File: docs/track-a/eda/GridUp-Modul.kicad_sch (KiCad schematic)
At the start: 54 parts, among them J1 İç ihtiyaç L / N / PE, J2 CT L1, J3 CT L2, J4 CT L3, J5 CT nötr, J6 Genişleme 2×5, J7 RS-485 klemens B / GND / A, J8 SMA panel, J9 Servis USB/UART0, SW1 Reset, U1 ESP32-S3-WROOM-1U-N8, U2 MLX90640ESF-BAA, U3 SHT31-DIS-B, U4 MAX3485, U5 RAC05-05SK/277, U6 AP7361C-33E 3,3 V / 1 A, U7 TPS61099 4,6 V

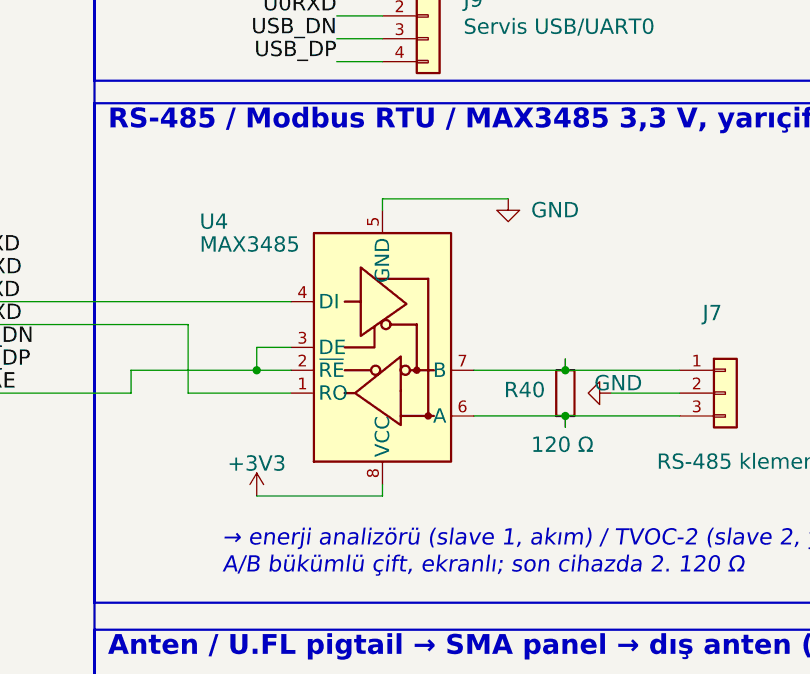
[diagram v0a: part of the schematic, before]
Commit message: İZ A: 03 — MAX3485 için sade kutu sembol (GridUp:MAX3485, aynı pin numaraları; kütüphane sembolü aynalanınca içi karışıyordu), ayna kaldırıldı, VCC üst / GND alt; ERC 0/0, netlist 103/103
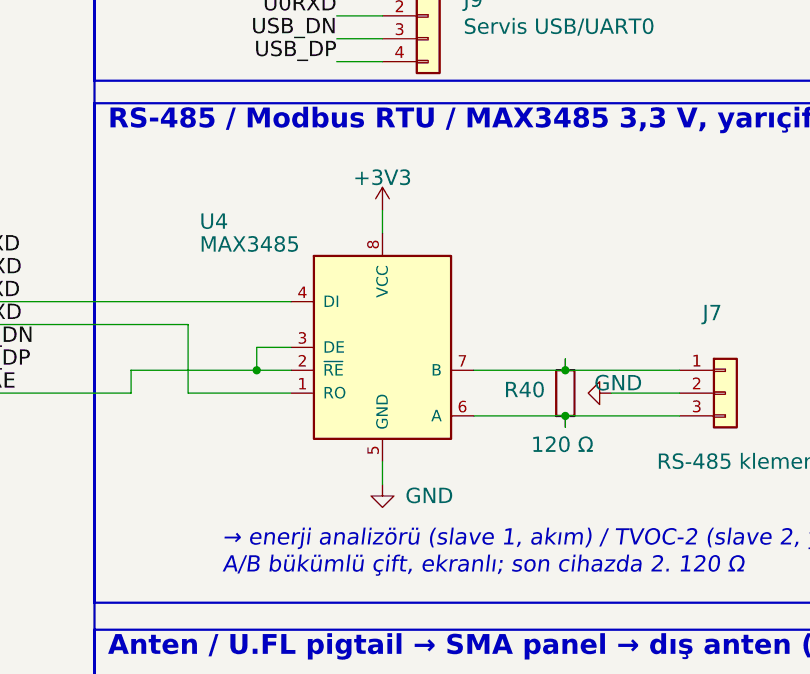
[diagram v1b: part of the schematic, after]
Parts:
- removed U4: MAX3485, Package_SO:SOIC-8_3.9x4.9mm_P1.27mm, symbol Interface_UART:MAX3485
- added U4: MAX3485, Package_SO:SOIC-8_3.9x4.9mm_P1.27mm, symbol GridUp:MAX3485
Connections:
- net +3V3: now also U4.8 (VCC)
- net DE_RE: now also U4.2 (~{RE}), U4.3 (DE)
- net GND: now also U4.5 (GND)
- net U1RXD: now also U4.1 (RO)
- net U1TXD: now also U4.4 (DI)
- net at J7.1 (Pin_1), R40.1: now also U4.7 (B)
- net at J7.3 (Pin_3), R40.2: now also U4.6 (A)
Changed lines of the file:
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@@
 	(wire
 		(pts
+			(xy 254 74.93)
 			(xy 254 72.39)
-			(xy 254 71.12)
-		)
-		(stroke
-			(width 0)
-			(type default)
-			(color 70 70 70 1)
-		)
-	)
-	(wire
-		(pts
-			(xy 254 71.12)
-			(xy 267.97 71.12)
-		)
-		(stroke
-			(width 0)
-			(type default)
-			(color 70 70 70 1)
-		)
-	)
-	(wire
-		(pts
-			(xy 254 102.87)
-			(xy 254 104.14)
 		)
 		(stroke
@@
 	(wire
 		(pts
-			(xy 254 104.14)
-			(xy 240.03 104.14)
+			(xy 254 100.33)
+			(xy 254 102.87)
 		)
 		(stroke
 			(width 0)
 			(type default)
-			(color 198 40 40 1)
+			(color 70 70 70 1)
 		)
 	)
@@
 	)
 	(symbol
-		(lib_id "Interface_UART:MAX3485")
+		(lib_id "GridUp:MAX3485")
 		(at 254 87.63 0)
-		(mirror x)
 		(unit 1)
 		(exclude_from_sim no)
@@
 			)
 		)
-		(pin "1"
-		)
-		(pin "2"
+		(pin "8"
 		)
-		(pin "3"
+		(pin "5"
 		)
 		(pin "4"
 		)
-		(pin "5"
+		(pin "3"
 		)
-		(pin "6"
+		(pin "2"
+		)
+		(pin "1"
 		)
 		(pin "7"
 		)
-		(pin "8"
+		(pin "6"
 		)
 		(instances
@@
 	)
 	(symbol
-		(lib_id "power:GND")
-		(at 267.97 71.12 0)
+		(lib_id "power:+3V3")
+		(at 254 72.39 0)
 		(unit 1)
 		(exclude_from_sim no)
@@
 		(dnp no)
 		(property "Reference" "#PWR22"
-			(at 270.51 68.58 0)
+			(at 256.54 69.85 0)
 			(hide yes)
 			(effects
@@
 					(size 1.7 1.7)
 				)
-				(justify left)
 			)
 		)
-		(property "Value" "GND"
-			(at 270.51 72.39 0)
+		(property "Value" "+3V3"
+			(at 254 68.79 0)
 			(effects
 				(font
 					(size 1.7 1.7)
 				)
-				(justify left)
 			)
 		)
 		(property "Footprint" ""
-			(at 267.97 71.12 0)
+			(at 254 72.39 0)
 			(hide yes)
 			(effects
@@
 					(size 1.7 1.7)
 				)
-				(justify left)
 			)
 		)
 		(property "Datasheet" ""
-			(at 267.97 71.12 0)
+			(at 254 72.39 0)
 			(hide yes)
 			(effects
@@
 					(size 1.7 1.7)
 				)
-				(justify left)
 			)
 		)
 		(property "Description" ""
-			(at 267.97 71.12 0)
+			(at 254 72.39 0)
 			(hide yes)
 			(effects
@@
 					(size 1.7 1.7)
 				)
-				(justify left)
 			)
 		)
@@
 	)
 	(symbol
-		(lib_id "power:+3V3")
-		(at 240.03 104.14 0)
+		(lib_id "power:GND")
+		(at 254 102.87 0)
 		(unit 1)
 		(exclude_from_sim no)
@@
 		(dnp no)
 		(property "Reference" "#PWR23"
-			(at 242.57 101.6 0)
+			(at 256.54 100.33 0)
 			(hide yes)
 			(effects
@@
 					(size 1.7 1.7)
 				)
+				(justify left)
 			)
 		)
-		(property "Value" "+3V3"
-			(at 240.03 100.54 0)
+		(property "Value" "GND"
+			(at 256.54 104.14 0)
 			(effects
 				(font
 					(size 1.7 1.7)
 				)
+				(justify left)
 			)
 		)
 		(property "Footprint" ""
-			(at 240.03 104.14 0)
+			(at 254 102.87 0)
 			(hide yes)
 			(effects
@@
 					(size 1.7 1.7)
 				)
+				(justify left)
 			)
 		)
 		(property "Datasheet" ""
-			(at 240.03 104.14 0)
+			(at 254 102.87 0)
 			(hide yes)
 			(effects
@@
 					(size 1.7 1.7)
 				)
+				(justify left)
 			)
 		)
 		(property "Description" ""
-			(at 240.03 104.14 0)
+			(at 254 102.87 0)
 			(hide yes)
 			(effects
@@
 					(size 1.7 1.7)
 				)
+				(justify left)
 			)
 		)

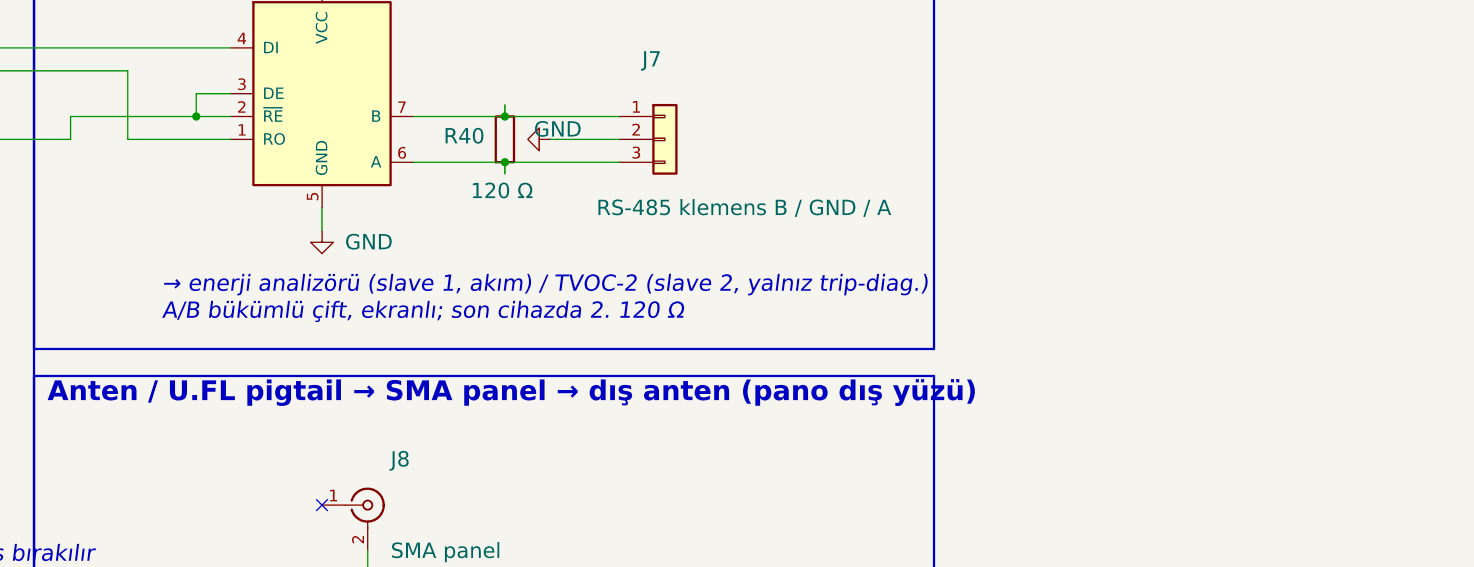
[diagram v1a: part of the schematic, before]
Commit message: İZ A: 03 — RS-485 notu 'hat: …' (sahipsiz ok kaldırıldı)
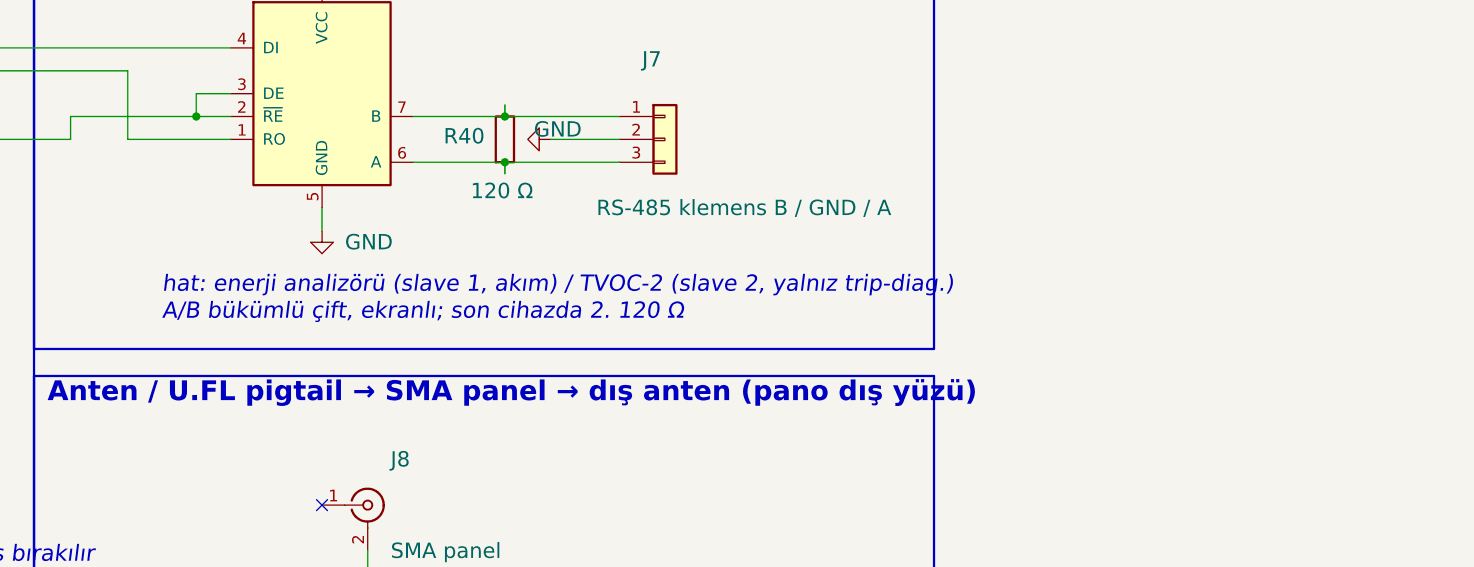
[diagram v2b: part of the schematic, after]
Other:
- note added: "hat: enerji analizörü (slave 1, akım) / TVOC-2 (slave 2, yalnız trip-diag.)"
- note removed: "→ enerji analizörü (slave 1, akım) / TVOC-2 (slave 2, yalnız trip-diag.)"
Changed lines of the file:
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@@
 		)
 	)
-	(text "→ enerji analizörü (slave 1, akım) / TVOC-2 (slave 2, yalnız trip-diag.)"
+	(text "hat: enerji analizörü (slave 1, akım) / TVOC-2 (slave 2, yalnız trip-diag.)"
 		(exclude_from_sim no)
 		(at 236.22 110 0)

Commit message: İZ A: 03 — J7 değeri pin numaralı: 1 B / 2 GND / 3 A
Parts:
- J7: value RS-485 klemens B / GND / A -> RS-485 klemens 1 B / 2 GND / 3 A
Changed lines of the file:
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@@
 			)
 		)
-		(property "Value" "RS-485 klemens B / GND / A"
+		(property "Value" "RS-485 klemens 1 B / 2 GND / 3 A"
 			(at 284.48 100.33 0)
 			(effects
